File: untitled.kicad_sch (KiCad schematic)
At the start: 10 parts, among them IC3 TPS63001DRCT, Q1 Q_PMOS

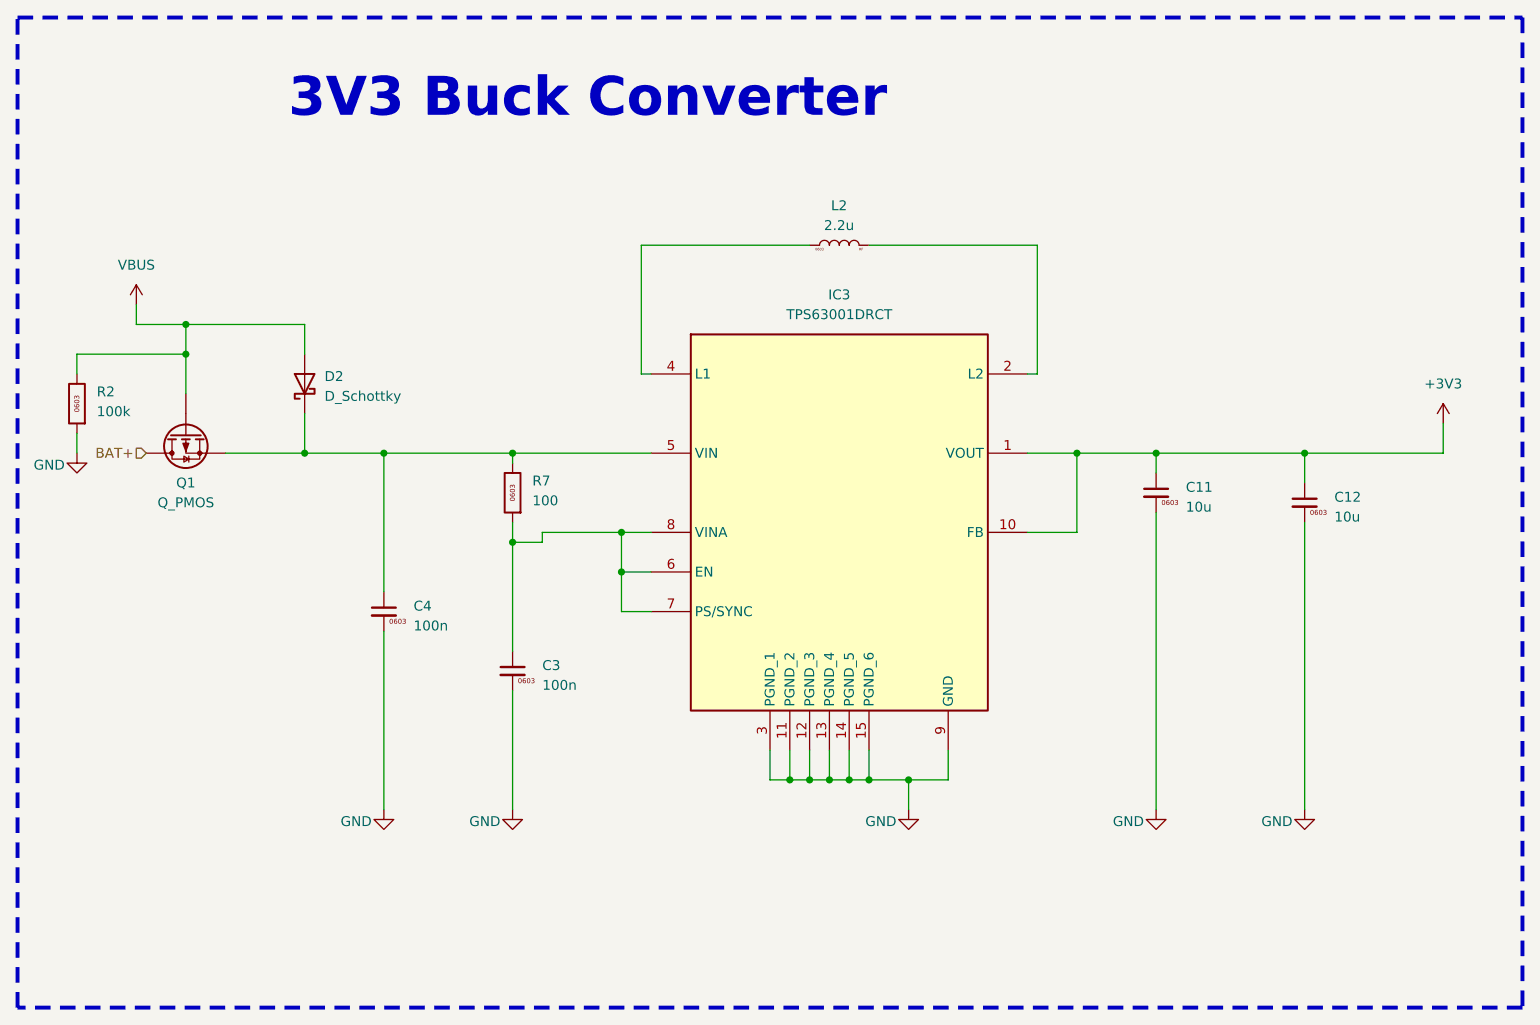
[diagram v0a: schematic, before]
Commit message: fix: Buck Converter inductor changed to the right type
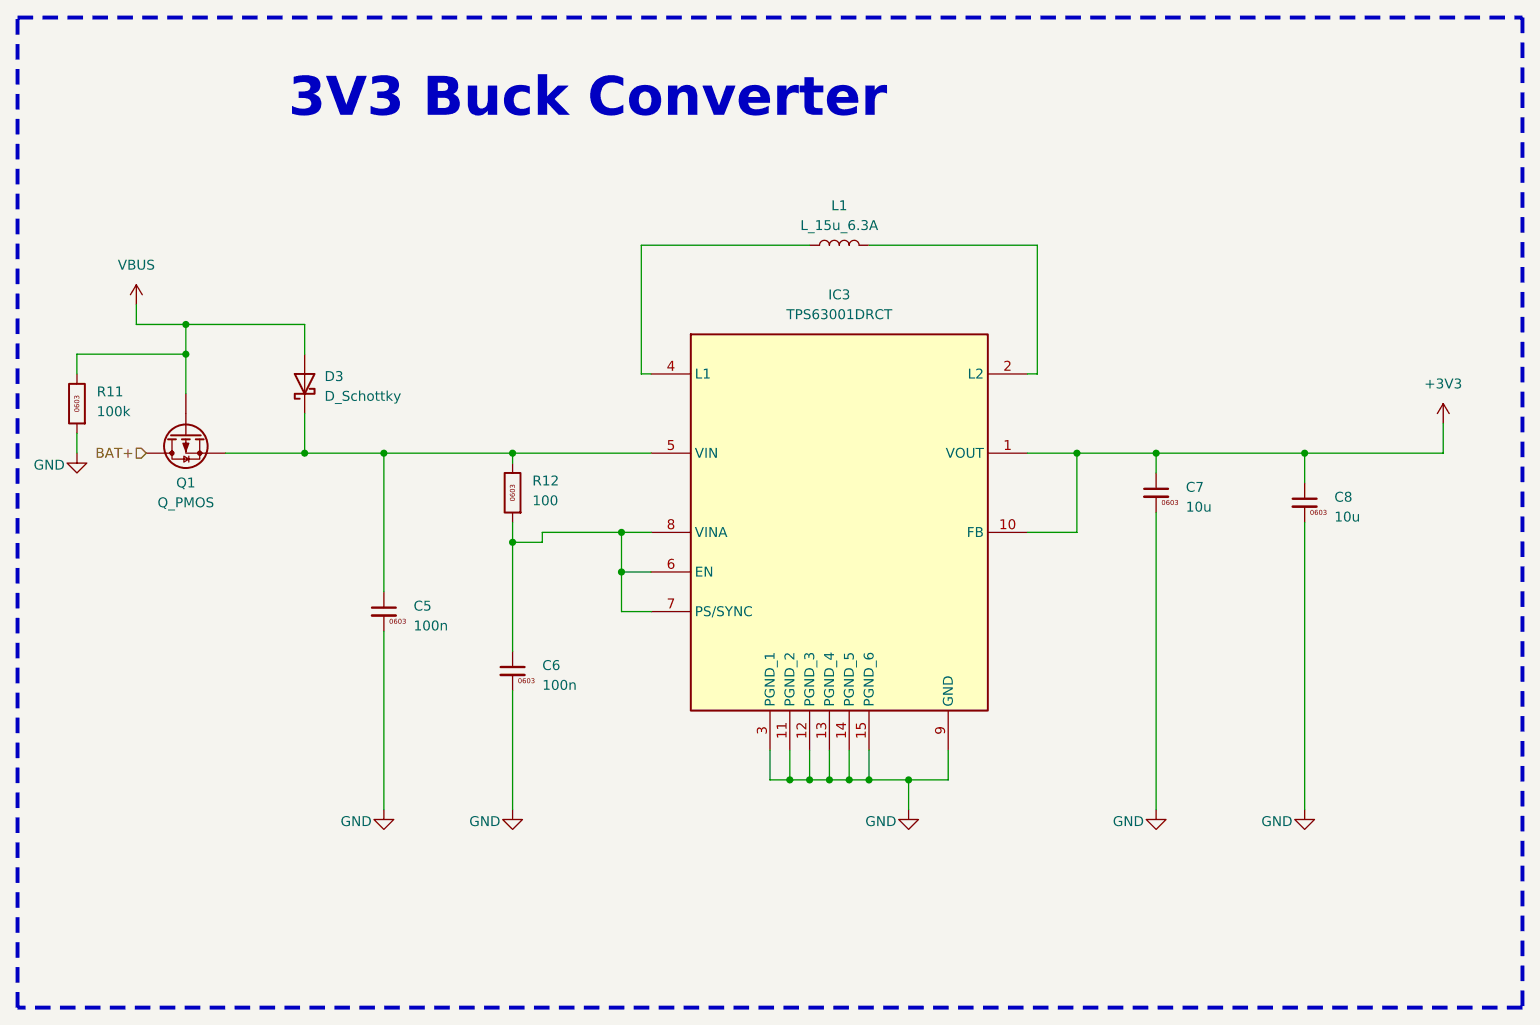
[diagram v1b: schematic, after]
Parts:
- removed L2: 2.2u, RolandsFootprint:L_0603_LQW_HandSolder, symbol Passive:L_27nH_LQW_RF
- added L1: L_15u_6.3A, BatteryCharger:VLS_EX, symbol Passive:L_15u_6.3A
- renumbered C4 to C5, C3 to C6, C11 to C7, C12 to C8, D2 to D3, R2 to R11, R7 to R12
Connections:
- net at IC3.2 (L2): now also L1.2
- net at IC3.4 (L1): now also L1.1
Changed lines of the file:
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@@
 		(on_board yes)
 		(dnp no)
-		(property "Reference" "R2"
+		(property "Reference" "R11"
 			(at 38.1 68.326 0)
 			(effects
@@
 			(project "projekt_Roland"
 				(path "/12081149-6dd0-47bb-bb21-fd1de250060f/233fb837-56b0-4e7b-900d-cd145004eaa8"
-					(reference "R2")
+					(reference "R11")
 					(unit 1)
 				)
@@
 		(dnp no)
 		(fields_autoplaced yes)
-		(property "Reference" "C12"
+		(property "Reference" "C8"
 			(at 196.85 81.8401 0)
 			(effects
@@
 			(project "projekt_Roland"
 				(path "/12081149-6dd0-47bb-bb21-fd1de250060f/233fb837-56b0-4e7b-900d-cd145004eaa8"
-					(reference "C12")
+					(reference "C8")
 					(unit 1)
 				)
@@
 		(on_board yes)
 		(dnp no)
-		(property "Reference" "R7"
+		(property "Reference" "R12"
 			(at 93.98 79.756 0)
 			(effects
@@
 			(project "projekt_Roland"
 				(path "/12081149-6dd0-47bb-bb21-fd1de250060f/233fb837-56b0-4e7b-900d-cd145004eaa8"
-					(reference "R7")
+					(reference "R12")
 					(unit 1)
 				)
@@
 		(dnp no)
 		(fields_autoplaced yes)
-		(property "Reference" "D2"
+		(property "Reference" "D3"
 			(at 67.31 66.3574 90)
 			(effects
@@
 			(project ""
 				(path "/12081149-6dd0-47bb-bb21-fd1de250060f/233fb837-56b0-4e7b-900d-cd145004eaa8"
-					(reference "D2")
+					(reference "D3")
 					(unit 1)
 				)
@@
 		(on_board yes)
 		(dnp no)
-		(property "Reference" "#PWR032"
+		(property "Reference" "#PWR033"
 			(at 193.04 128.27 0)
 			(effects
@@
 			(project "projekt_Roland"
 				(path "/12081149-6dd0-47bb-bb21-fd1de250060f/233fb837-56b0-4e7b-900d-cd145004eaa8"
-					(reference "#PWR032")
+					(reference "#PWR033")
 					(unit 1)
 				)
@@
 		(dnp no)
 		(fields_autoplaced yes)
-		(property "Reference" "C3"
+		(property "Reference" "C6"
 			(at 95.25 103.4301 0)
 			(effects
@@
 			(project "projekt_Roland"
 				(path "/12081149-6dd0-47bb-bb21-fd1de250060f/233fb837-56b0-4e7b-900d-cd145004eaa8"
-					(reference "C3")
+					(reference "C6")
 					(unit 1)
 				)
@@
 		(dnp no)
 		(fields_autoplaced yes)
-		(property "Reference" "#PWR033"
+		(property "Reference" "#PWR034"
 			(at 210.82 76.2 0)
 			(effects
@@
 			(project "projekt_Roland"
 				(path "/12081149-6dd0-47bb-bb21-fd1de250060f/233fb837-56b0-4e7b-900d-cd145004eaa8"
-					(reference "#PWR033")
+					(reference "#PWR034")
 					(unit 1)
 				)
@@
 		(on_board yes)
 		(dnp no)
-		(property "Reference" "#PWR013"
+		(property "Reference" "#PWR027"
 			(at 35.56 82.55 0)
 			(effects
@@
 			(project "projekt_Roland"
 				(path "/12081149-6dd0-47bb-bb21-fd1de250060f/233fb837-56b0-4e7b-900d-cd145004eaa8"
-					(reference "#PWR013")
+					(reference "#PWR027")
 					(unit 1)
 				)
@@
 		(on_board yes)
 		(dnp no)
-		(property "Reference" "#PWR031"
+		(property "Reference" "#PWR032"
 			(at 173.99 128.27 0)
 			(effects
@@
 			(project "projekt_Roland"
 				(path "/12081149-6dd0-47bb-bb21-fd1de250060f/233fb837-56b0-4e7b-900d-cd145004eaa8"
-					(reference "#PWR031")
-					(unit 1)
-				)
-			)
-		)
-	)
-	(symbol
-		(lib_id "Passive:L_27nH_LQW_RF")
+					(reference "#PWR032")
+					(unit 1)
+				)
+			)
+		)
+	)
+	(symbol
+		(lib_id "Passive:L_15u_6.3A")
 		(at 133.35 49.53 90)
 		(unit 1)
@@
 		(dnp no)
 		(fields_autoplaced yes)
-		(property "Reference" "L2"
-			(at 133.3219 44.45 90)
-			(effects
-				(font
-					(size 1.27 1.27)
-				)
-			)
-		)
-		(property "Value" "2.2u"
-			(at 133.3219 46.99 90)
-			(effects
-				(font
-					(size 1.27 1.27)
-				)
-			)
-		)
-		(property "Footprint" "RolandsFootprint:L_0603_LQW_HandSolder"
-			(at 133.35 49.53 0)
-			(effects
-				(font
-					(size 1.27 1.27)
-				)
-				(hide yes)
-			)
-		)
-		(property "Datasheet" "~"
-			(at 128.27 49.53 0)
-			(effects
-				(font
-					(size 1.27 1.27)
-				)
-				(hide yes)
-			)
-		)
-		(property "Description" "Inductor"
-			(at 125.73 59.69 0)
-			(effects
-				(font
-					(size 1.27 1.27)
-				)
-				(hide yes)
-			)
+		(property "Reference" "L1"
+			(at 133.35 44.45 90)
+			(effects
+				(font
+					(size 1.27 1.27)
+				)
+			)
+		)
+		(property "Value" "L_15u_6.3A"
+			(at 133.35 46.99 90)
+			(effects
+				(font
+					(size 1.27 1.27)
+				)
+			)
+		)
+		(property "Footprint" "BatteryCharger:VLS_EX"
+			(at 120.65 49.276 0)
+			(effects
+				(font
+					(size 1.27 1.27)
+				)
+				(hide yes)
+			)
+		)
+		(property "Datasheet" "https://product.tdk.com/system/files/dam/doc/product/inductor/inductor/smd/catalog/inductor_commercial_power_vls5045ex_en.pdf"
+			(at 151.638 17.018 0)
+			(effects
+				(font
+					(size 1.27 1.27)
+				)
+				(hide yes)
+			)
+		)
+		(property "Description" "Inductor 15uH 6.3A 40 mOhm SMD"
+			(at 149.606 43.942 0)
+			(effects
+				(font
+					(size 1.27 1.27)
+				)
+				(hide yes)
+			)
+		)
+		(property "MOC" "VLS5045EX-2R2N"
+			(at 147.574 52.324 0)
+			(effects
+				(font
+					(size 1.27 1.27)
+				)
+				(hide yes)
+			)
+		)
+		(property "Supplier" "TME"
+			(at 145.034 50.8 0)
+			(effects
+				(font
+					(size 1.27 1.27)
+				)
+				(hide yes)
+			)
+		)
+		(property "Size" "11.5×10.3×4.0"
+			(at 153.924 55.626 0)
+			(effects
+				(font
+					(size 1.27 1.27)
+				)
+				(hide yes)
+			)
+		)
+		(property "TME" "VLS5045EX-2R2N"
+			(at 133.35 49.53 90)
+			(effects
+				(font
+					(size 1.27 1.27)
+				)
+				(hide yes)
+			)
+		)
+		(pin "1"
 		)
 		(pin "2"
 		)
-		(pin "1"
-		)
-		(instances
-			(project "projekt_Roland"
-				(path "/12081149-6dd0-47bb-bb21-fd1de250060f/233fb837-56b0-4e7b-900d-cd145004eaa8"
-					(reference "L2")
+		(instances
+			(project ""
+				(path "/12081149-6dd0-47bb-bb21-fd1de250060f/233fb837-56b0-4e7b-900d-cd145004eaa8"
+					(reference "L1")
 					(unit 1)
 				)
@@
 		(on_board yes)
 		(dnp no)
-		(property "Reference" "#PWR029"
+		(property "Reference" "#PWR030"
 			(at 91.44 128.27 0)
 			(effects
@@
 			(project "projekt_Roland"
 				(path "/12081149-6dd0-47bb-bb21-fd1de250060f/233fb837-56b0-4e7b-900d-cd145004eaa8"
-					(reference "#PWR029")
+					(reference "#PWR030")
 					(unit 1)
 				)
@@
 		(dnp no)
 		(fields_autoplaced yes)
-		(property "Reference" "C11"
+		(property "Reference" "C7"
 			(at 177.8 80.5701 0)
 			(effects
@@
 			(project "projekt_Roland"
 				(path "/12081149-6dd0-47bb-bb21-fd1de250060f/233fb837-56b0-4e7b-900d-cd145004eaa8"
-					(reference "C11")
+					(reference "C7")
 					(unit 1)
 				)
@@
 		(on_board yes)
 		(dnp no)
-		(property "Reference" "#PWR018"
+		(property "Reference" "#PWR031"
 			(at 142.24 128.27 0)
 			(effects
@@
 			(project "projekt_Roland"
 				(path "/12081149-6dd0-47bb-bb21-fd1de250060f/233fb837-56b0-4e7b-900d-cd145004eaa8"
-					(reference "#PWR018")
+					(reference "#PWR031")
 					(unit 1)
 				)
@@
 		(dnp no)
 		(fields_autoplaced yes)
-		(property "Reference" "#PWR04"
+		(property "Reference" "#PWR028"
 			(at 43.18 60.96 0)
 			(effects
@@
 			(project ""
 				(path "/12081149-6dd0-47bb-bb21-fd1de250060f/233fb837-56b0-4e7b-900d-cd145004eaa8"
-					(reference "#PWR04")
+					(reference "#PWR028")
 					(unit 1)
 				)
@@
 		(dnp no)
 		(fields_autoplaced yes)
-		(property "Reference" "C4"
+		(property "Reference" "C5"
 			(at 78.74 95.8101 0)
 			(effects
@@
 			(project "projekt_Roland"
 				(path "/12081149-6dd0-47bb-bb21-fd1de250060f/233fb837-56b0-4e7b-900d-cd145004eaa8"
-					(reference "C4")
+					(reference "C5")
 					(unit 1)
 				)
@@
 		(on_board yes)
 		(dnp no)
-		(property "Reference" "#PWR030"
+		(property "Reference" "#PWR029"
 			(at 74.93 128.27 0)
 			(effects
@@
 			(project "projekt_Roland"
 				(path "/12081149-6dd0-47bb-bb21-fd1de250060f/233fb837-56b0-4e7b-900d-cd145004eaa8"
-					(reference "#PWR030")
-					(unit 1)
-				)
+					(reference "#PWR029")
+					(unit 1)
+				)
